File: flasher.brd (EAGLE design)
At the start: 54 x 62.6 mm, 37 parts, among them IC2 TINY85-20-DIP, Q1 2N2222, U1 CL2N3, U2 CL2N3, U3 CL2N3, U4 CL2N3, U5 CL2N3, U6 CL2N3

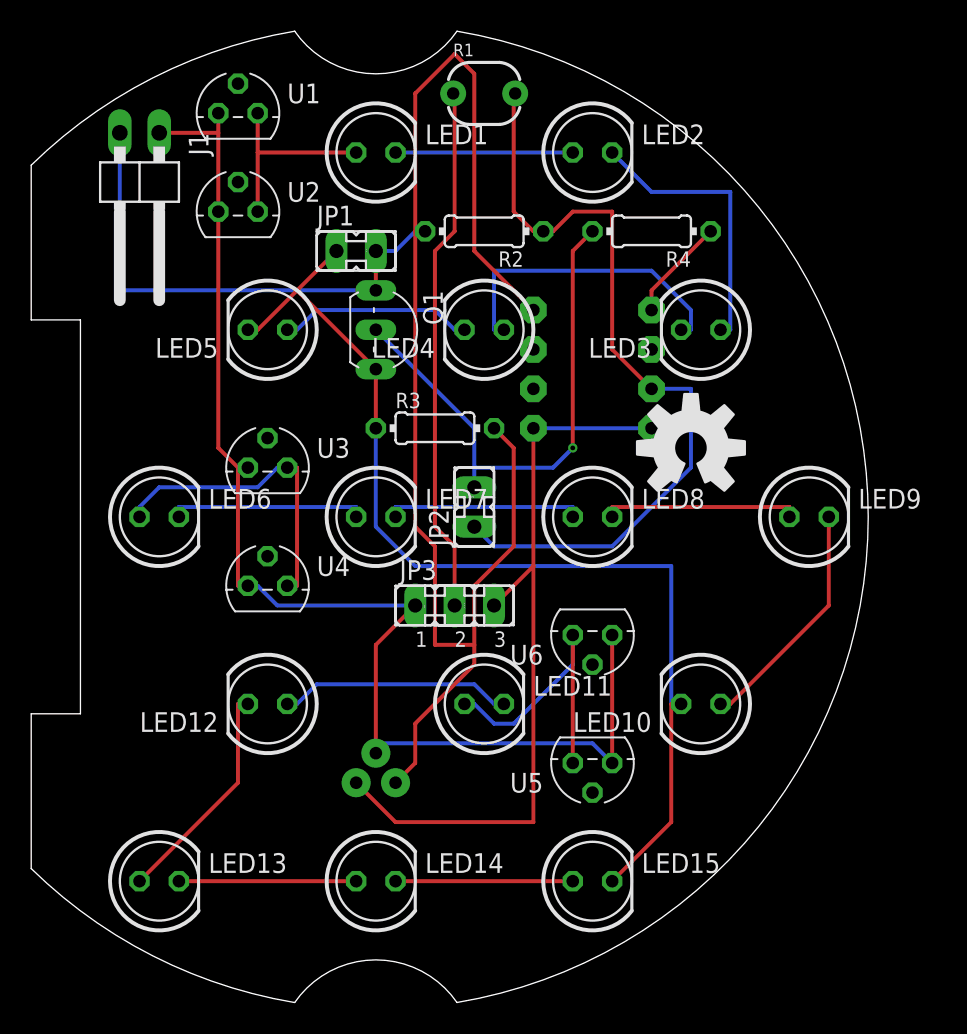
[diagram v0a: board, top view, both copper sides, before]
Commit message: Final version, so far - brought flasher to ready for manufacture - done away with Pro assembly variant, not feasible - made design more robust, doing away with power resistor - sorted top silk, added branding and extra artwork - made flip-compatible (can be assembled as left or right hand side using same PCB)
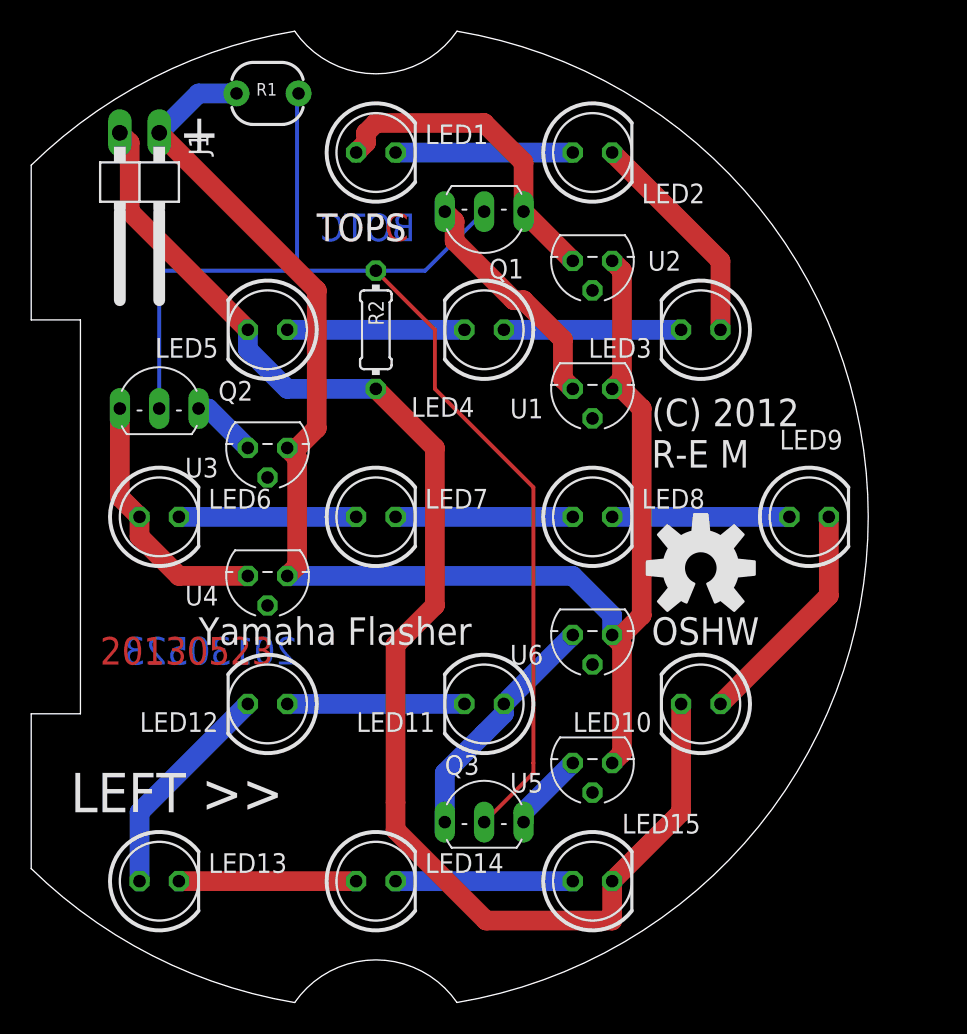
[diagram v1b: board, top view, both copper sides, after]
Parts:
- removed IC1: (no value), SparkFun-PowerIC:TO-92
- removed IC2: TINY85-20-DIP, SparkFun-DigitalIC:DIP08
- removed JP1, JP2: (no value), jumper:JP1
- removed JP1C, JP2C, JP3C1, JP3C2: (no value), jumper:JUMP
- removed JP3: (no value), jumper:JP2
- removed R3: 220, 1/2W, rcl:0204/7
- removed R4: 2K2, rcl:0204/7
- added Q2, Q3: 2N2222, transistor-neu-to92:TO92-EBC
- J1: value (none) -> POWER
- moved U1 29.0 mm to (36.8, 40.6), turned to 180 degrees
- moved U2 23.1 mm to (36.8, 48.9), turned to 180 degrees
- moved R1 14.0 mm to (15.9, 59.7)
- moved R2 9.44 mm to (22.9, 44.5), turned to 270 degrees
- moved Q1 8.54 mm to (29.8, 50.8), turned to 180 degrees
- moved LOGO1 7.77 mm to (43.8, 29.1)
- moved U3 1.27 mm to (15.9, 36.8), turned to 180 degrees
- moved U4 0.63 mm to (15.9, 28.6), turned to 180 degrees
- turned LED11 to 180 degrees
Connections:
- removed net COMMAND: JP2.2, Q1.B, R4.2
- removed net N$19: JP1.1, LED10.K, LED15.K, LED5.K, Q1.C, R3.1
- net GND: now also LED10.K, LED15.K, LED5.K; no longer IC1.1, IC2.4, JP1.2, Q1.E, R3.2
- net N$11: now also Q2.E; no longer U3.3
- net N$13: now also Q3.C, U5.3; no longer JP3.2, R1.1
- net N$17: now also Q3.E; no longer U5.3
- net N$4: now also Q1.E; no longer U1.3
- net N$6: now also Q1.C, U1.3; no longer IC2.5, R4.1
- net N$7: now also Q2.C, U3.3; no longer IC1.3, IC2.1, IC2.8, JP3.3
- net SENSE: now also Q1.B, Q2.B, Q3.B; no longer IC2.7, JP2.1
- net VCC: now also R1.1; no longer IC1.2, JP3.1
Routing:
- net N$19: track 68.4 -> 0.00 mm
- net N$7: track 49.1 -> 4.23 mm
- net COMMAND: track 34.2 -> 0.00 mm, vias 1 -> 0
- net SENSE: track 51.8 -> 84.0 mm
- net GND: track 121.6 -> 90.0 mm
- net N$13: track 34.2 -> 5.13 mm
- net VCC: track 83.3 -> 99.5 mm
- net N$3: track 20.1 -> 11.4 mm
- net N$6: track 6.66 -> 15.2 mm
- net N$4: track 12.7 -> 20.7 mm
- net N$2: track 18.2 -> 14.3 mm
- net N$17: track 19.2 -> 15.5 mm
- net N$14: track 15.0 -> 11.4 mm
- net N$11: track 20.1 -> 16.8 mm
- net N$9: track 12.7 -> 11.4 mm
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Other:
- board text added: "(C) 2012 R-E M"
- board text added: "+"
- board text added: "20130523"
- board text added: "<< RIGHT"
- board text added: "A"
- board text added: "BOTC"
- board text added: "BOTS"
- board text added: "E"
- board text added: "LEFT >>"
- board text added: "O"
- board text added: "OSHW"
- board text added: "TOPC"
- board text added: "TOPS"
- board text added: "Yamaha Flasher"

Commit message: Final version, so far - brought tail/brake to ready for manufacture - two assembly versions: simple and dimmed - sorted top/bottom silk, added branding and extra artwork
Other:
- board text added: "(C) 2013 R-E M"
- board text removed: "(C) 2012 R-E M"
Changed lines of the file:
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@@
 <text x="25.4" y="50.165" size="1.778" layer="16" font="vector" ratio="15" rot="MR0">BOTC</text>
 <text x="11.43" y="24.13" size="1.778" layer="21" font="vector" ratio="15">Yamaha Flasher</text>
-<text x="40.64" y="35.56" size="1.778" layer="21" font="vector" ratio="15">(C) 2012
+<text x="40.64" y="35.56" size="1.778" layer="21" font="vector" ratio="15">(C) 2013
 R-E M</text>
 </plain>

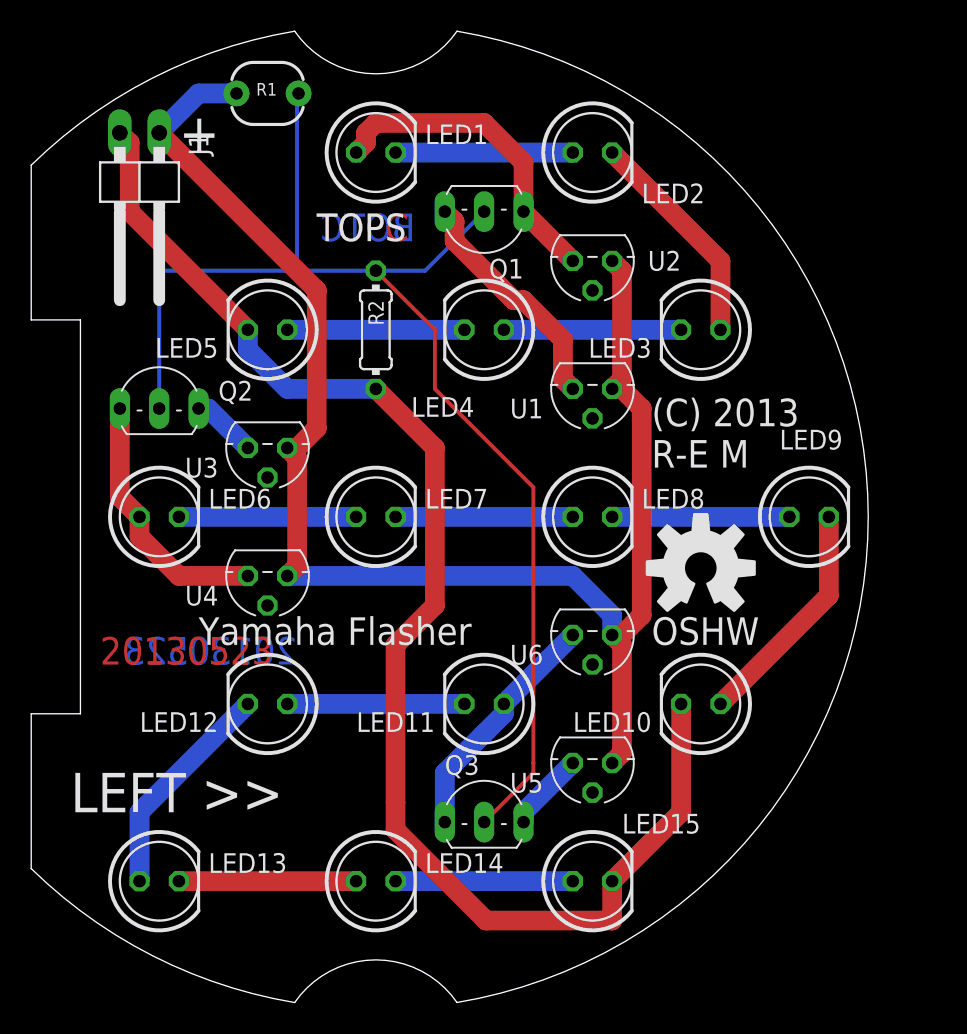
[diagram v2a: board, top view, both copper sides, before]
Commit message: BUGFIX: - added 0.1uF as recommended by Supertex CL2N3 datasheet - rotated power connector to make it more accessible during assembly
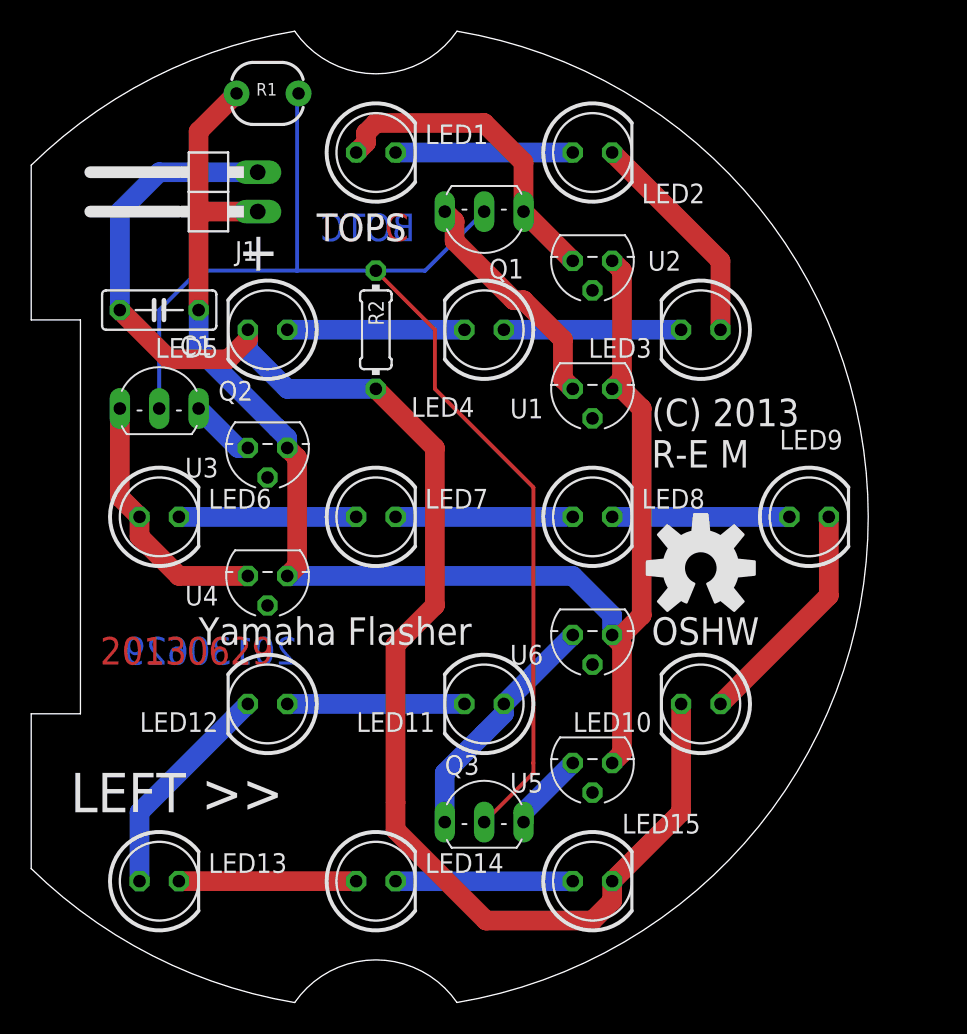
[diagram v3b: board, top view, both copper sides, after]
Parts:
- added C1: 100nF, rcl:C050-025X075
- moved J1 3.81 mm to (11.4, 53.3), turned to 90 degrees
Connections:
- net GND: now also C1.2
- net VCC: now also C1.1
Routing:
- net GND: track 90.0 -> 100.1 mm
- net VCC: track 99.5 -> 97.9 mm
- net SENSE: track 84.0 -> 82.5 mm
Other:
- board text added: "20130629"
- board text removed: "20130523"
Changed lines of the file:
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@@
 <wire x1="0.635" y1="45.085" x2="3.81" y2="45.085" width="0.0254" layer="20"/>
 <wire x1="0.635" y1="45.085" x2="0.635" y2="55.0672" width="0.0254" layer="20"/>
-<text x="10.16" y="55.88" size="2.54" layer="21" font="vector" ratio="15">+</text>
-<text x="11.938" y="55.88" size="2.54" layer="22" font="vector" ratio="15" rot="MR0">+</text>
+<text x="13.97" y="48.26" size="2.54" layer="21" font="vector" ratio="15">+</text>
+<text x="15.748" y="48.26" size="2.54" layer="22" font="vector" ratio="15" rot="MR0">+</text>
 <text x="3.175" y="13.335" size="2.54" layer="21" font="vector" ratio="15">LEFT &gt;&gt;</text>
 <text x="19.05" y="13.335" size="2.54" layer="22" font="vector" ratio="15" rot="MR0">&lt;&lt; RIGHT</text>
 <text x="40.64" y="24.13" size="1.778" layer="21" font="vector" ratio="15">OSHW</text>
-<text x="5.08" y="22.86" size="1.778" layer="1" font="vector" ratio="15">20130523</text>
-<text x="17.78" y="22.86" size="1.778" layer="16" font="vector" ratio="15" rot="MR0">20130523</text>
+<text x="5.08" y="22.86" size="1.778" layer="1" font="vector" ratio="15">20130629</text>
+<text x="17.78" y="22.86" size="1.778" layer="16" font="vector" ratio="15" rot="MR0">20130629</text>
 <text x="19.05" y="54.61" size="1.778" layer="22" font="vector" ratio="15" rot="MR0">A</text>
 <text x="33.02" y="54.61" size="1.778" layer="22" font="vector" ratio="15" rot="MR0">A</text>
@@
 <element name="U6" library="radu-collected" package="TO-92" value="CL2N3" x="36.83" y="24.765" rot="R180"/>
 <element name="LOGO1" library="SparkFun-Aesthetics" package="OSHW-LOGO-L" value="OSHW-LOGOL" x="43.815" y="29.083"/>
-<element name="J1" library="pinhead" package="1X02/90" value="POWER" x="7.62" y="53.34" rot="R180"/>
+<element name="J1" library="pinhead" package="1X02/90" value="POWER" x="11.43" y="53.34" rot="R90"/>
 <element name="Q2" library="transistor-neu-to92" package="TO92-EBC" value="2N2222" x="8.89" y="40.64" smashed="yes">
 <attribute name="NAME" x="12.7" y="39.878" size="1.27" layer="25" ratio="10"/>
@@
 <variant name="Simple" populate="no"/>
 </element>
+<element name="C1" library="rcl" package="C050-025X075" value="100nF" x="8.89" y="45.72" rot="R180"/>
 </elements>
 <signals>
@@
 <wire x1="17.145" y1="40.64" x2="14.605" y2="43.18" width="1.27" layer="16"/>
 <wire x1="14.605" y1="43.18" x2="14.605" y2="44.45" width="1.27" layer="16"/>
-<wire x1="6.985" y1="56.515" x2="6.35" y2="57.15" width="1.27" layer="1"/>
-<wire x1="6.985" y1="52.07" x2="6.985" y2="56.515" width="1.27" layer="1"/>
-<wire x1="14.605" y1="44.45" x2="6.985" y2="52.07" width="1.27" layer="1"/>
 <wire x1="22.86" y1="40.64" x2="26.67" y2="36.83" width="1.27" layer="1"/>
 <wire x1="26.67" y1="36.83" x2="26.67" y2="26.67" width="1.27" layer="1"/>
@@
 <wire x1="24.13" y1="13.97" x2="24.13" y2="12.192" width="1.27" layer="1"/>
 <wire x1="24.13" y1="12.192" x2="29.972" y2="6.35" width="1.27" layer="1"/>
-<wire x1="29.972" y1="6.35" x2="38.1" y2="6.35" width="1.27" layer="1"/>
-<wire x1="38.1" y1="6.35" x2="38.1" y2="8.89" width="1.27" layer="1"/>
+<wire x1="29.972" y1="6.35" x2="36.83" y2="6.35" width="1.27" layer="1"/>
+<wire x1="36.83" y1="6.35" x2="38.1" y2="7.62" width="1.27" layer="1"/>
+<wire x1="38.1" y1="7.62" x2="38.1" y2="8.89" width="1.27" layer="1"/>
+<contactref element="C1" pad="2"/>
+<wire x1="15.24" y1="54.61" x2="8.89" y2="54.61" width="1.27" layer="16"/>
+<wire x1="8.89" y1="54.61" x2="6.35" y2="52.07" width="1.27" layer="16"/>
+<wire x1="6.35" y1="52.07" x2="6.35" y2="45.72" width="1.27" layer="16"/>
+<wire x1="9.525" y1="42.545" x2="6.35" y2="45.72" width="1.27" layer="1"/>
+<wire x1="14.605" y1="44.45" x2="14.605" y2="43.815" width="1.27" layer="1"/>
+<wire x1="14.605" y1="43.815" x2="13.335" y2="42.545" width="1.27" layer="1"/>
+<wire x1="13.335" y1="42.545" x2="9.525" y2="42.545" width="1.27" layer="1"/>
 </signal>
 <signal name="VCC" class="1">
@@
 <contactref element="J1" pad="1"/>
 <contactref element="R1" pad="1"/>
-<wire x1="11.43" y1="59.69" x2="8.89" y2="57.15" width="1.27" layer="16"/>
-<wire x1="13.335" y1="59.69" x2="11.43" y2="59.69" width="1.27" layer="16"/>
-<wire x1="13.335" y1="59.69" x2="13.875" y2="59.69" width="1.27" layer="16"/>
 <wire x1="38.735" y1="41.275" x2="38.1" y2="40.64" width="1.27" layer="1"/>
 <wire x1="38.735" y1="48.26" x2="38.735" y2="41.275" width="1.27" layer="1"/>
@@
 <wire x1="38.735" y1="40.64" x2="38.1" y2="40.64" width="1.27" layer="1"/>
 <wire x1="38.735" y1="24.765" x2="38.1" y2="24.765" width="1.27" layer="1"/>
-<wire x1="19.05" y1="46.99" x2="8.89" y2="57.15" width="1.27" layer="1"/>
-<wire x1="19.05" y1="38.1" x2="19.05" y2="46.99" width="1.27" layer="1"/>
-<wire x1="17.78" y1="36.83" x2="19.05" y2="38.1" width="1.27" layer="1"/>
-<wire x1="17.78" y1="36.83" x2="17.145" y2="36.83" width="1.27" layer="1"/>
+<contactref element="C1" pad="1"/>
+<wire x1="13.875" y1="59.69" x2="11.43" y2="57.245" width="1.27" layer="1"/>
+<wire x1="11.43" y1="57.245" x2="11.43" y2="52.07" width="1.27" layer="1"/>
+<wire x1="11.43" y1="52.07" x2="11.43" y2="45.72" width="1.27" layer="1"/>
+<wire x1="15.24" y1="52.07" x2="11.43" y2="52.07" width="1.27" layer="1"/>
+<wire x1="11.43" y1="45.72" x2="11.43" y2="43.18" width="1.27" layer="16"/>
+<wire x1="11.43" y1="43.18" x2="16.51" y2="38.1" width="1.27" layer="16"/>
+<wire x1="16.51" y1="38.1" x2="17.145" y2="37.465" width="1.27" layer="16"/>
+<wire x1="17.145" y1="37.465" x2="17.145" y2="36.83" width="1.27" layer="16"/>
 </signal>
 <signal name="SENSE" class="2">
@@
 <contactref element="Q1" pad="B"/>
 <contactref element="R1" pad="2"/>
-<wire x1="8.89" y1="48.26" x2="8.89" y2="39.37" width="0.254" layer="16"/>
+<wire x1="17.78" y1="48.26" x2="11.43" y2="48.26" width="0.254" layer="16"/>
+<wire x1="11.43" y1="48.26" x2="8.89" y2="45.72" width="0.254" layer="16"/>
+<wire x1="8.89" y1="45.72" x2="8.89" y2="39.37" width="0.254" layer="16"/>
 <wire x1="22.86" y1="48.26" x2="17.78" y2="48.26" width="0.254" layer="16"/>
-<wire x1="17.78" y1="48.26" x2="8.89" y2="48.26" width="0.254" layer="16"/>
 <wire x1="26.035" y1="48.26" x2="29.845" y2="52.07" width="0.254" layer="16"/>
 <wire x1="22.86" y1="48.26" x2="26.035" y2="48.26" width="0.254" layer="16"/>
@@
 <contactref element="Q2" pad="C"/>
 <contactref element="U3" pad="3"/>
-<wire x1="12.065" y1="39.37" x2="14.605" y2="36.83" width="1.27" layer="16"/>
-<wire x1="11.43" y1="39.37" x2="12.065" y2="39.37" width="1.27" layer="16"/>
+<wire x1="14.605" y1="36.83" x2="13.97" y2="36.83" width="1.27" layer="16"/>
+<wire x1="13.97" y1="36.83" x2="11.43" y2="39.37" width="1.27" layer="16"/>
 </signal>
 <signal name="N$13" class="1">
